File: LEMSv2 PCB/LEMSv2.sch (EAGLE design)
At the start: 63 parts, among them J2 M05, J7 FEMALE 2x3, Q1 200mA/50V, Q2 200mA/50V, Q3 200mA/50V, Q4 200mA/50V, Q5 200mA/50V, Q6 200mA/50V, Q7 200mA/50V, Q8 MMBT3904, Q9 MMBT3904, U1 SDMMC06132, U2 DS3231/SO, U3 TLV2372, U4 BMP280

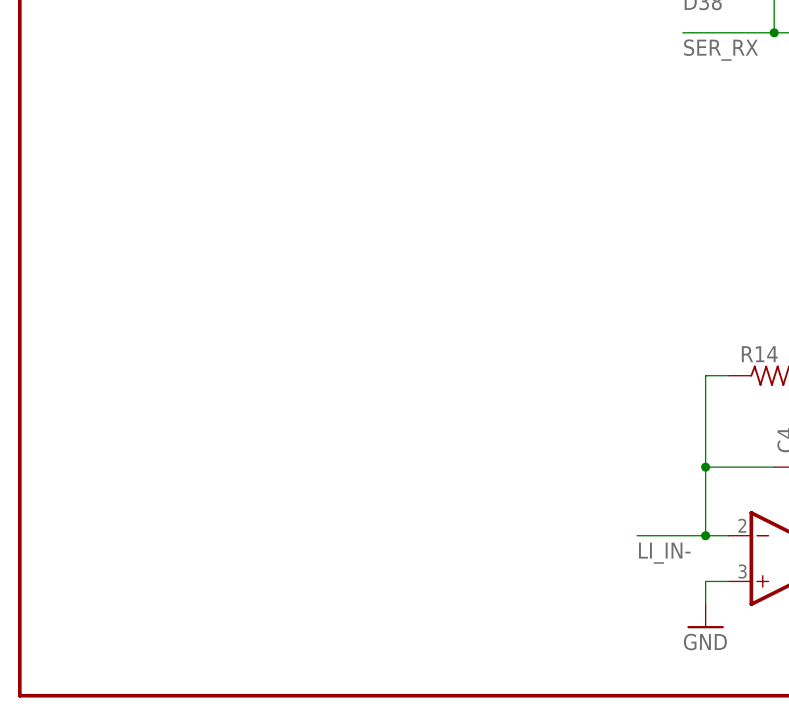
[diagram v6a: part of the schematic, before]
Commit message: Added ADC and support parts
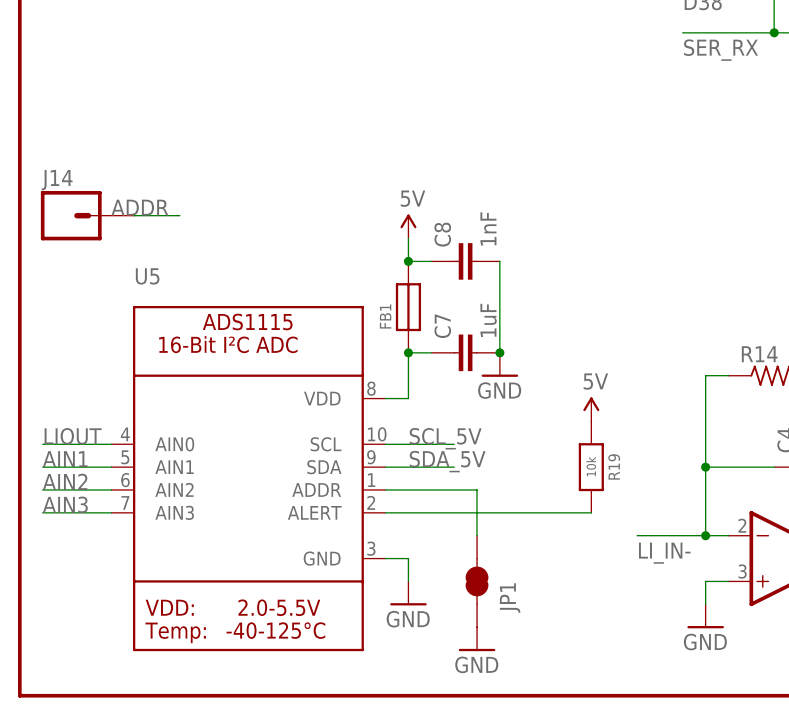
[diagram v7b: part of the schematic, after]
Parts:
- added C7: 1uF, LEMSv2:CAP0805
- added C8: 1nF, LEMSv2:CAP0805
- added FB1: FERRITE, LEMSv2:FERRITE
- added J14: (no value), SparkFun-Connectors:M01PTH
- added JP1: JUMPER-PAD-2-NC_BY_TRACE, SparkFun-Passives:JUMPER-PAD-2-NC_BY_TRACE
- added R19: 10k, LEMSv2:RESISTOR_0805
- added U5: (no value), LEMSv2:ADC_ADS1115
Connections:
- new net ADDR: J14.1, JP1.1, U5.ADDR
- new net AIN1: U5.AIN1
- new net AIN2: U5.AIN2
- new net AIN3: U5.AIN3
- new net ALERT: R19.2, U5.ALERT
- new net N$14: C7.1, FB1.P$1, U5.VDD
- net 5V: now also C8.1, FB1.P$2, R19.1
- net GND: now also C7.2, C8.2, JP1.2, U5.GND
- net LIOUT: now also U5.AIN0
- net SCL_5V: now also U5.SCL
- net SDA_5V: now also U5.SDA
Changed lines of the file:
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@@
 <part name="SUPPLY11" library="LEMSv2" deviceset="3.3V" device=""/>
 <part name="SUPPLY12" library="LEMSv2" deviceset="3.3V" device=""/>
+<part name="FB1" library="LEMSv2" deviceset="FERRITE" device=""/>
+<part name="U5" library="LEMSv2" deviceset="ADC_ADS1115" device=""/>
+<part name="C7" library="LEMSv2" deviceset="CAP" device="0805" value="1uF"/>
+<part name="C8" library="LEMSv2" deviceset="CAP" device="0805" value="1nF"/>
+<part name="SUPPLY13" library="LEMSv2" deviceset="5V" device=""/>
+<part name="GND10" library="LEMSv2" deviceset="GND" device=""/>
+<part name="GND11" library="LEMSv2" deviceset="GND" device=""/>
+<part name="R19" library="LEMSv2" deviceset="RESISTOR" device="_0805" value="10k"/>
+<part name="JP1" library="SparkFun-Passives" deviceset="JUMPER-PAD-2-NC_BY_TRACE" device=""/>
+<part name="J14" library="SparkFun-Connectors" deviceset="M01" device="PTH"/>
+<part name="GND12" library="LEMSv2" deviceset="GND" device=""/>
+<part name="SUPPLY14" library="LEMSv2" deviceset="5V" device=""/>
 </parts>
 <sheets>
@@
 <instance part="SUPPLY11" gate="G$1" x="20.32" y="137.16"/>
 <instance part="SUPPLY12" gate="G$1" x="55.88" y="137.16"/>
+<instance part="FB1" gate="G$1" x="43.18" y="43.18" smashed="yes" rot="R90">
+<attribute name="NAME" x="41.275" y="40.64" size="1.27" layer="95" rot="R90"/>
+</instance>
+<instance part="U5" gate="G$1" x="25.4" y="25.4"/>
+<instance part="C7" gate="G$1" x="50.8" y="38.1" rot="R90"/>
+<instance part="C8" gate="G$1" x="50.8" y="48.26" rot="R90"/>
+<instance part="SUPPLY13" gate="G$1" x="43.18" y="50.8"/>
+<instance part="GND10" gate="1" x="43.18" y="10.16"/>
+<instance part="GND11" gate="1" x="53.34" y="35.56"/>
+<instance part="R19" gate="G$1" x="63.5" y="25.4" rot="R270"/>
+<instance part="JP1" gate="G$1" x="50.8" y="12.7" smashed="yes" rot="R270">
+<attribute name="NAME" x="53.34" y="12.7" size="1.778" layer="95" rot="R270"/>
+</instance>
+<instance part="J14" gate="G$1" x="5.08" y="53.34"/>
+<instance part="GND12" gate="1" x="50.8" y="5.08"/>
+<instance part="SUPPLY14" gate="G$1" x="63.5" y="30.48"/>
 </instances>
 <busses>
@@
 <pinref part="GND9" gate="1" pin="GND"/>
 </segment>
+<segment>
+<pinref part="C8" gate="G$1" pin="2"/>
+<pinref part="C7" gate="G$1" pin="2"/>
+<wire x1="53.34" y1="48.26" x2="53.34" y2="38.1" width="0.1524" layer="91"/>
+<pinref part="GND11" gate="1" pin="GND"/>
+<junction x="53.34" y="38.1"/>
+</segment>
+<segment>
+<pinref part="U5" gate="G$1" pin="GND"/>
+<pinref part="GND10" gate="1" pin="GND"/>
+<wire x1="40.64" y1="15.24" x2="43.18" y2="15.24" width="0.1524" layer="91"/>
+<wire x1="43.18" y1="15.24" x2="43.18" y2="12.7" width="0.1524" layer="91"/>
+</segment>
+<segment>
+<pinref part="JP1" gate="G$1" pin="2"/>
+<pinref part="GND12" gate="1" pin="GND"/>
+</segment>
 </net>
 <net name="SCK" class="0">
@@
 <wire x1="137.16" y1="22.86" x2="137.16" y2="20.32" width="0.1524" layer="91"/>
 <junction x="129.54" y="22.86"/>
+</segment>
+<segment>
+<pinref part="FB1" gate="G$1" pin="P$2"/>
+<pinref part="SUPPLY13" gate="G$1" pin="5V"/>
+<wire x1="43.18" y1="48.26" x2="43.18" y2="50.8" width="0.1524" layer="91"/>
+<pinref part="C8" gate="G$1" pin="1"/>
+<wire x1="43.18" y1="48.26" x2="45.72" y2="48.26" width="0.1524" layer="91"/>
+<junction x="43.18" y="48.26"/>
+</segment>
+<segment>
+<pinref part="R19" gate="G$1" pin="1"/>
+<pinref part="SUPPLY14" gate="G$1" pin="5V"/>
 </segment>
 </net>
@@
 <junction x="238.76" y="104.14"/>
 </segment>
+<segment>
+<pinref part="U5" gate="G$1" pin="SCL"/>
+<wire x1="40.64" y1="27.94" x2="48.26" y2="27.94" width="0.1524" layer="91"/>
+<label x="43.18" y="27.94" size="1.778" layer="95"/>
+</segment>
 </net>
 <net name="SDA_5V" class="0">
@@
 <wire x1="243.84" y1="106.68" x2="243.84" y2="99.06" width="0.1524" layer="91"/>
 <junction x="243.84" y="99.06"/>
+</segment>
+<segment>
+<pinref part="U5" gate="G$1" pin="SDA"/>
+<wire x1="40.64" y1="25.4" x2="48.26" y2="25.4" width="0.1524" layer="91"/>
+<label x="43.18" y="25.4" size="1.778" layer="95"/>
 </segment>
 </net>
@@
 <wire x1="93.98" y1="35.56" x2="93.98" y2="25.4" width="0.1524" layer="91"/>
 <junction x="93.98" y="25.4"/>
+</segment>
+<segment>
+<pinref part="U5" gate="G$1" pin="AIN0"/>
+<wire x1="10.16" y1="27.94" x2="2.54" y2="27.94" width="0.1524" layer="91"/>
+<label x="2.54" y="27.94" size="1.778" layer="95"/>
 </segment>
 </net>
@@
 </segment>
 </net>
+<net name="AIN1" class="0">
+<segment>
+<pinref part="U5" gate="G$1" pin="AIN1"/>
+<wire x1="10.16" y1="25.4" x2="2.54" y2="25.4" width="0.1524" layer="91"/>
+<label x="2.54" y="25.4" size="1.778" layer="95"/>
+</segment>
+</net>
+<net name="AIN2" class="0">
+<segment>
+<pinref part="U5" gate="G$1" pin="AIN2"/>
+<wire x1="10.16" y1="22.86" x2="2.54" y2="22.86" width="0.1524" layer="91"/>
+<label x="2.54" y="22.86" size="1.778" layer="95"/>
+</segment>
+</net>
+<net name="AIN3" class="0">
+<segment>
+<pinref part="U5" gate="G$1" pin="AIN3"/>
+<wire x1="10.16" y1="20.32" x2="2.54" y2="20.32" width="0.1524" layer="91"/>
+<label x="2.54" y="20.32" size="1.778" layer="95"/>
+</segment>
+</net>
+<net name="N$14" class="0">
+<segment>
+<pinref part="FB1" gate="G$1" pin="P$1"/>
+<pinref part="C7" gate="G$1" pin="1"/>
+<wire x1="43.18" y1="38.1" x2="45.72" y2="38.1" width="0.1524" layer="91"/>
+<junction x="43.18" y="38.1"/>
+<pinref part="U5" gate="G$1" pin="VDD"/>
+<wire x1="40.64" y1="33.02" x2="43.18" y2="33.02" width="0.1524" layer="91"/>
+<wire x1="43.18" y1="33.02" x2="43.18" y2="38.1" width="0.1524" layer="91"/>
+</segment>
+</net>
+<net name="ALERT" class="0">
+<segment>
+<pinref part="U5" gate="G$1" pin="ALERT"/>
+<pinref part="R19" gate="G$1" pin="2"/>
+<wire x1="40.64" y1="20.32" x2="63.5" y2="20.32" width="0.1524" layer="91"/>
+</segment>
+</net>
+<net name="ADDR" class="0">
+<segment>
+<pinref part="J14" gate="G$1" pin="1"/>
+<wire x1="12.7" y1="53.34" x2="17.78" y2="53.34" width="0.1524" layer="91"/>
+<label x="10.16" y="53.34" size="1.778" layer="95"/>
+</segment>
+<segment>
+<pinref part="U5" gate="G$1" pin="ADDR"/>
+<pinref part="JP1" gate="G$1" pin="1"/>
+<wire x1="40.64" y1="22.86" x2="50.8" y2="22.86" width="0.1524" layer="91"/>
+<wire x1="50.8" y1="22.86" x2="50.8" y2="17.78" width="0.1524" layer="91"/>
+</segment>
+</net>

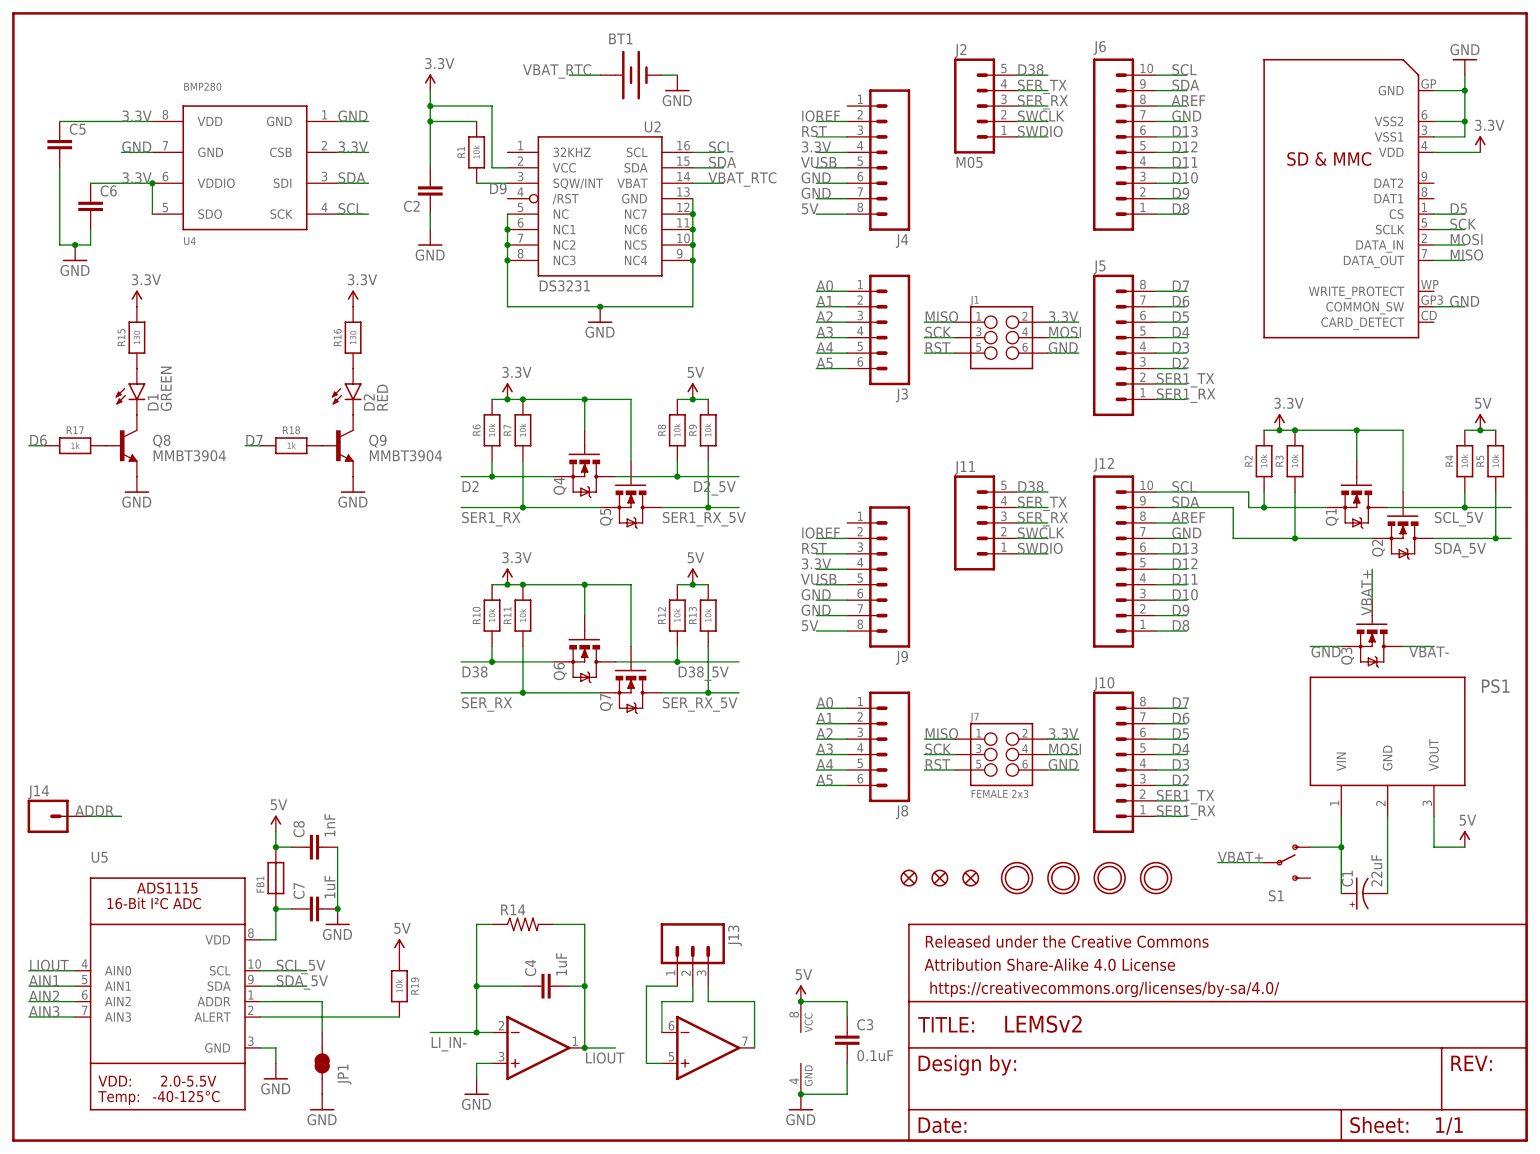
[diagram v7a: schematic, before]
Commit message: Added final schematic parts
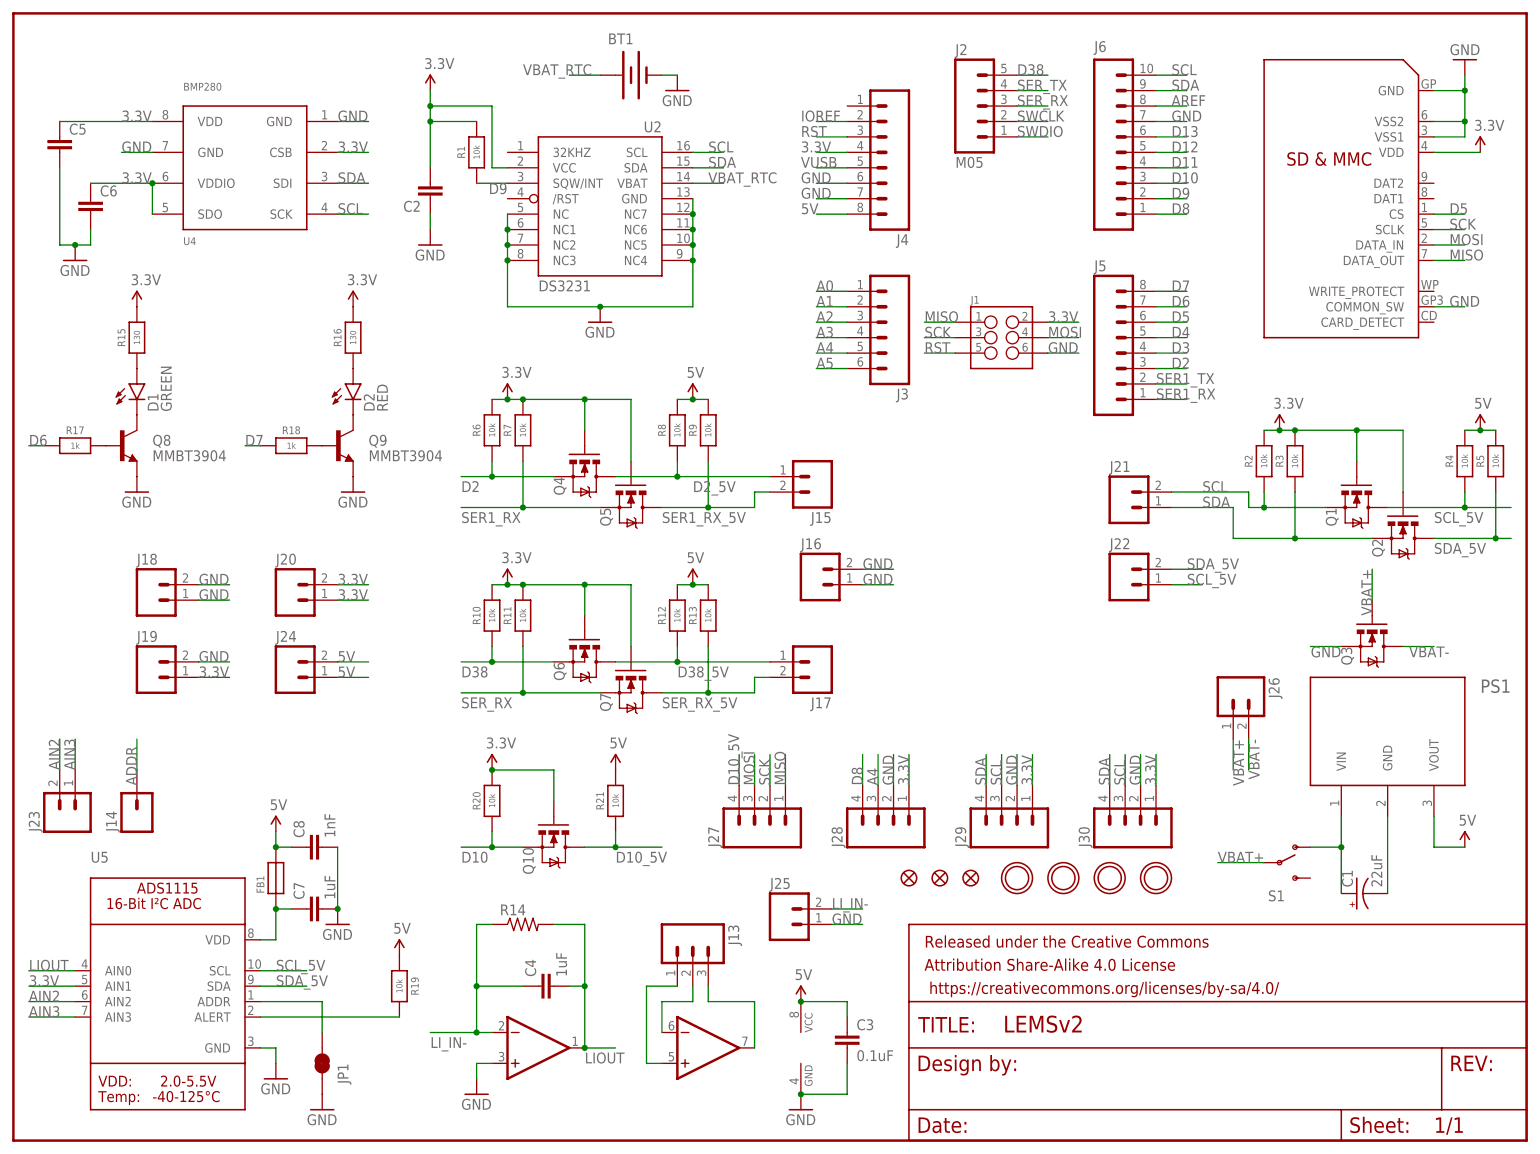
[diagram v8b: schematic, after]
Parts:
- removed J10, J9: (no value), LEMSv2:M08LOCK
- removed J11: (no value), LEMSv2:M05_SFLOCK
- removed J12: (no value), LEMSv2:M10LOCK
- removed J7: FEMALE 2x3, LEMSv2:M03X2FEMALE
- removed J8: (no value), LEMSv2:M06LOCK
- added J15, J16, J17, J18, J19, J20, J21, J22, J23, J24, J25, J26: (no value), LEMSv2:M023.5MM
- added J27, J28, J29, J30: (no value), LEMSv2:M04SCREW
- added Q10: 200mA/50V, LEMSv2:MOSFET-NCHANNELBSS138
- added R20, R21: 10k, LEMSv2:RESISTOR_0805
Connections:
- removed net AIN1: U5.AIN1
- new net D10_5V: J27.4, Q10.D, R21.1
- net 3.3V: now also J19.1, J20.1, J20.2, J28.1, J29.1, J30.1, Q10.G, R20.2, U5.AIN1; no longer J7.2, J9.4
- net 5V: now also J24.1, J24.2, R21.2; no longer J9.8
- net A0: no longer J8.1
- net A1: no longer J8.2
- net A2: no longer J8.3
- net A3: no longer J8.4
- net A4: now also J28.3; no longer J8.5
- net A5: no longer J8.6
- net AIN2: now also J23.2
- net AIN3: now also J23.1
- net AREF: no longer J12.8
- net D10: now also Q10.S, R20.1; no longer J12.3
- net D11: no longer J12.4
- net D12: no longer J12.5
- net D13: no longer J12.6
- net D2: no longer J10.3
- net D2_5V: now also J15.1
- net D3: no longer J10.4
- net D38: no longer J11.5
- net D38_5V: now also J17.1
- net D4: no longer J10.5
- net D5: no longer J10.6
- net D6: no longer J10.7
- net D7: no longer J10.8
- net D8: now also J28.4; no longer J12.1
- net D9: no longer J12.2
- net GND: now also J16.1, J16.2, J18.1, J18.2, J19.2, J25.1, J28.2, J29.2, J30.2; no longer J12.7, J7.6, J9.6, J9.7
- net IOREF: no longer J9.2
- net LI_IN-: now also J25.2
- net MISO: now also J27.1; no longer J7.1
- net MOSI: now also J27.3; no longer J7.4
- net RST: no longer J7.5, J9.3
- net SCK: now also J27.2; no longer J7.3
- net SCL: now also J21.2, J29.3, J30.3; no longer J12.10
- net SCL_5V: now also J22.1
- net SDA: now also J21.1, J29.4, J30.4; no longer J12.9
- net SDA_5V: now also J22.2
- net SER1_RX: no longer J10.1
- net SER1_RX_5V: now also J15.2
- net SER1_TX: no longer J10.2
- net SER_RX: no longer J11.3
- net SER_RX_5V: now also J17.2
- net SER_TX: no longer J11.4
- net SWCLK: no longer J11.2
- net SWDIO: no longer J11.1
- net VBAT+: now also J26.1
- net VBAT-: now also J26.2
- net VUSB: no longer J9.5
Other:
- moved on the sheet: J14
